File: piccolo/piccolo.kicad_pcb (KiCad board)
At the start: 2 copper layers, 136.6 x 20.6 mm, 21 parts, among them U1 ProMicro

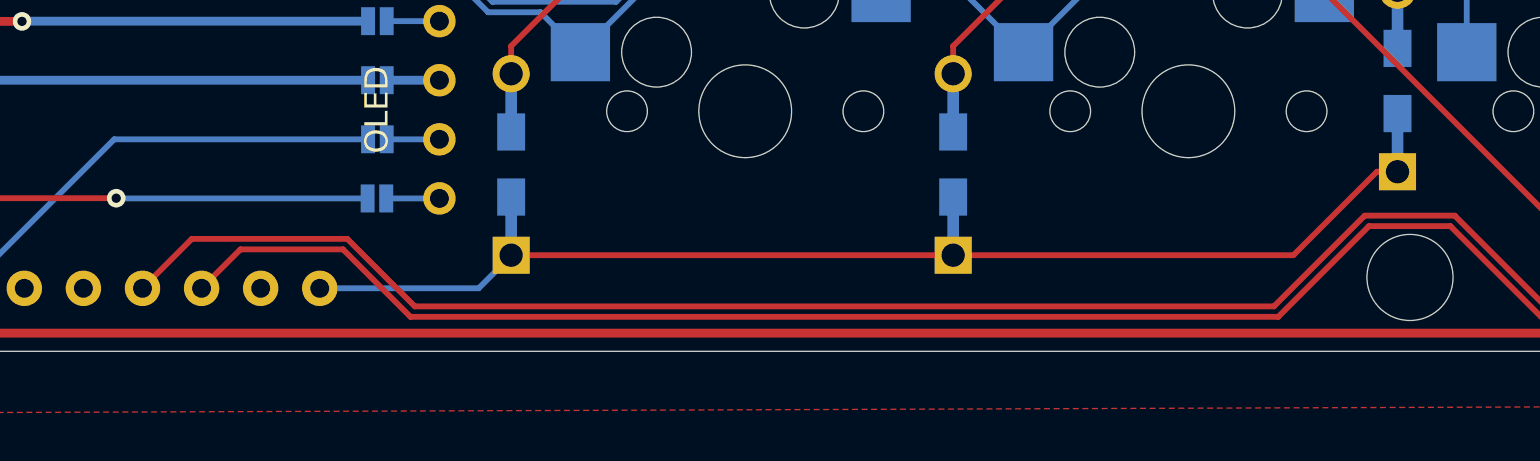
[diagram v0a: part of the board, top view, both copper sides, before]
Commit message: Added switchplate and backplate
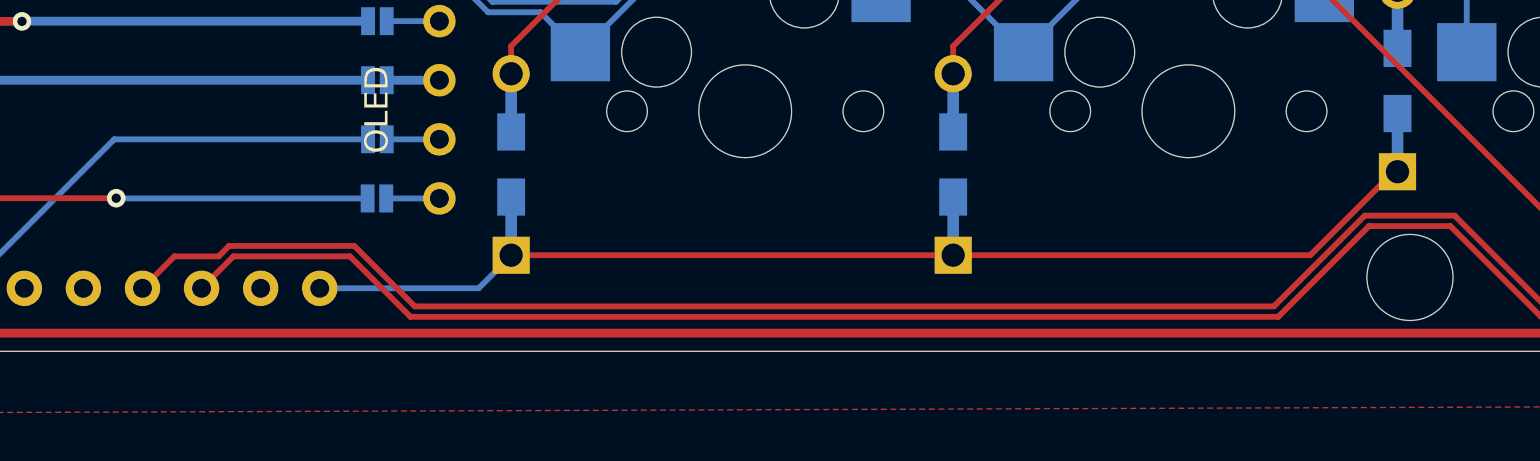
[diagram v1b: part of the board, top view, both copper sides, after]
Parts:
- removed REF** (x3): MountingHole_3.7mm, MountingHole:MountingHole_3.7mm
- added H1: MountingHole, Envoy:ClearanceHole_3.7mm, F.Cu at (87.3, 42.1)
- added H2: MountingHole, Envoy:ClearanceHole_3.7mm, F.Cu at (125.4, 56.4)
- added H3: MountingHole, Envoy:ClearanceHole_3.7mm, F.Cu at (163.5, 42.1)

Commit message: Add PCB identifier and revision number
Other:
- board text added: "Piccolo Macro Pad by JeJeff rev 0.2"
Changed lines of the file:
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@@
   (gr_arc (start 47.52975 39.6875) (end 47.52975 38.89375) (angle -90) (layer "Edge.Cuts") (width 0.05))
   (gr_arc (start 182.5625 58.7375) (end 182.5625 59.53125) (angle -90) (layer "Edge.Cuts") (width 0.05))
+  (gr_text "Piccolo Macro Pad\nby JeJeff\nrev 0.2" (at 56.1 49.55) (layer "F.Mask")
+    (effects (font (size 1 1) (thickness 0.15)) (justify left))
+  )
   (dimension (type aligned) (layer "Dwgs.User")
     (pts (xy 182.5625 59.53125) (xy 182.5625 38.89375))
